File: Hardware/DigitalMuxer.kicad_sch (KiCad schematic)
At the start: 20 parts, among them SW1 Push_Button, SW2 Push_Button, SW3 Push_Button, SW4 Push_Button, SW5 Slide Switch, U2 PCF8574APWR

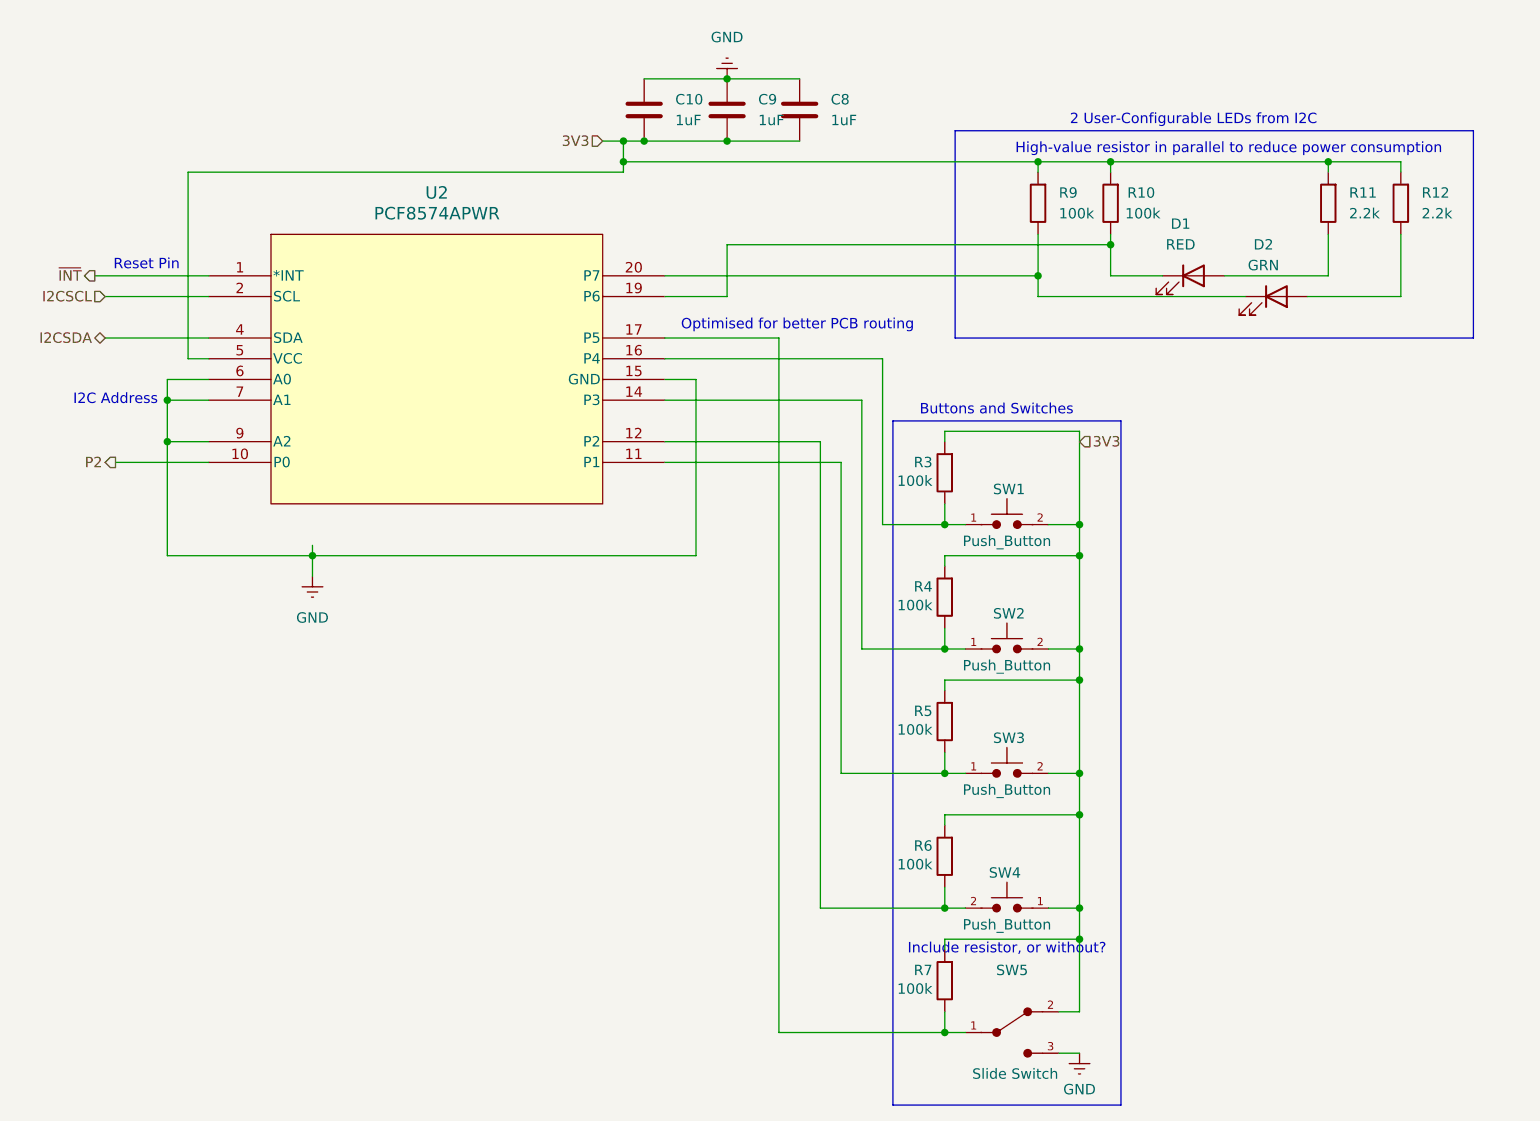
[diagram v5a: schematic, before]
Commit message: Initial OS architecture, and updated PCB work After a joint planning session, designed and architected OS structure: ``` src/ |- os: Audio, Accelerometer, Humidity, etc |- drivers: I2C interfaces, per-chip ```
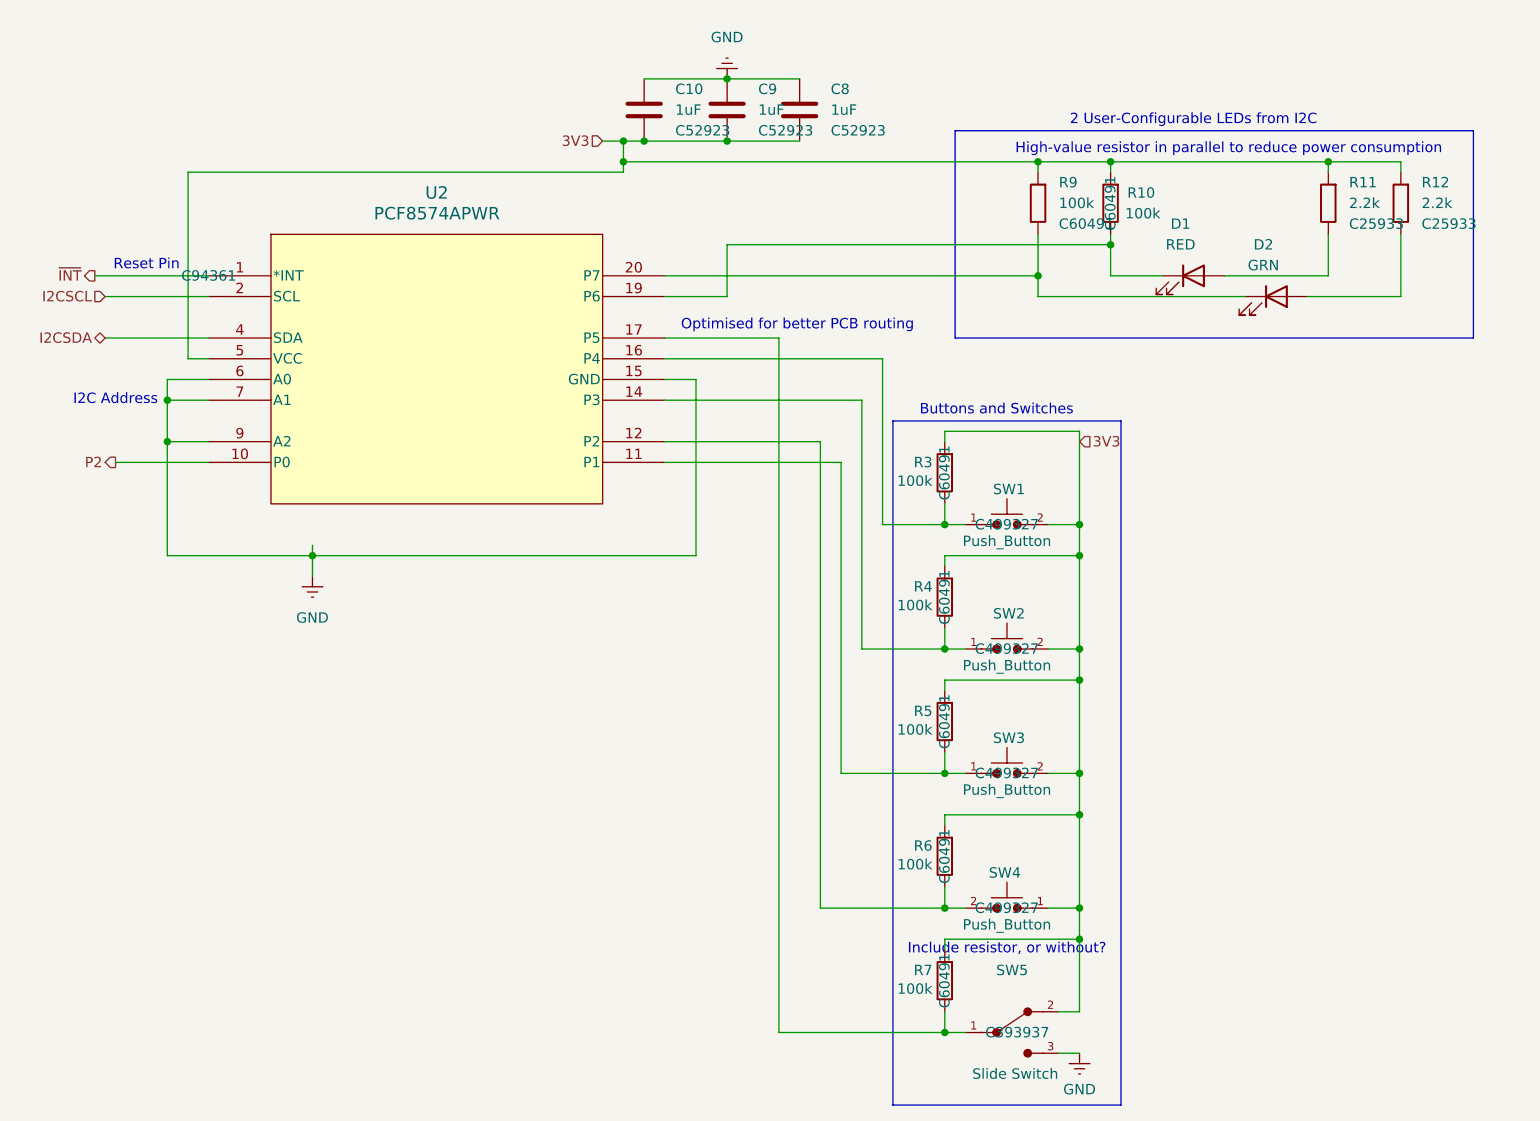
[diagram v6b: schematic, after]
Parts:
- C10, C8, C9: footprint Resistor_SMD:R_01005_0402Metric -> Capacitor_SMD:C_0402_1005Metric; symbol Peanut:C -> Peanut:C 1uF; LCSC (none) -> C52923
- R10, R3, R4, R5, R6, R7, R9: symbol Peanut:R -> Peanut:R 100k; LCSC (none) -> C60491
- R11, R12: symbol Peanut:R -> Peanut:R 2.2k; LCSC (none) -> C25933
- SW1, SW2, SW3, SW4: LCSC (none) -> C499327
- SW5: LCSC (none) -> C393937
- U2: LCSC (none) -> C94361

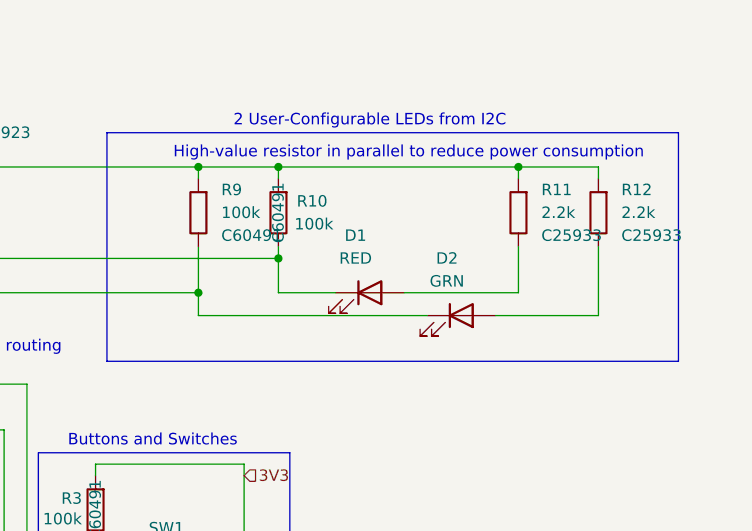
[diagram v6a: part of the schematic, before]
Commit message: Updates to PCB and ADC Schematics
- Swapped audio jack to correct pin (4P-DIP)
- Add LCSC numbers for all components
- Reroute some sensitive signal traces
- Add Board rev and author
- add 4x M2 mounting holes
- fixup some misc silkscreen, footprints, and component 3d models
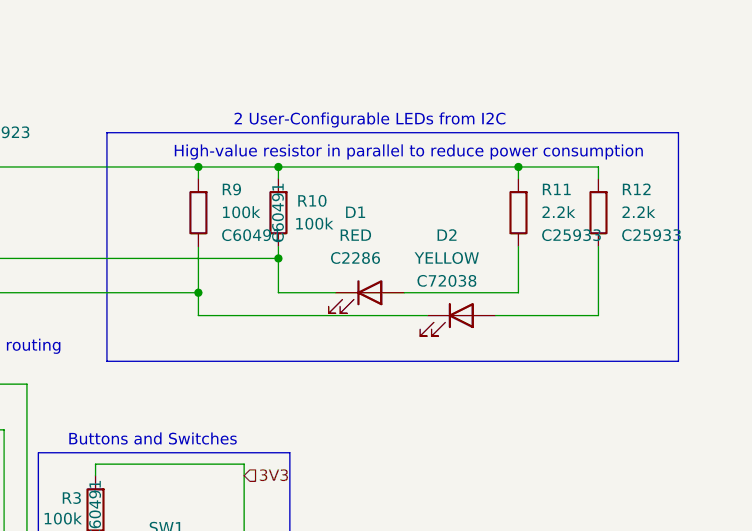
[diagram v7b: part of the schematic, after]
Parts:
- D1: footprint LED_SMD:LED_0201_0603Metric -> LED_SMD:LED_0603_1608Metric; symbol Peanut:LED -> Peanut:LED Red; LCSC (none) -> C2286
- D2: value GRN -> YELLOW; footprint LED_SMD:LED_0201_0603Metric -> LED_SMD:LED_0603_1608Metric; symbol Peanut:LED -> Peanut:LED Yellow; LCSC (none) -> C72038
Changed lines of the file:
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@@
 			)
 		)
-		(property "Description" "Unpolarized capacitor"
+		(property "Description" "Capacitor 1uF"
 			(at 111.76 38.1 0)
 			(effects
@@
 	)
 	(symbol
-		(lib_id "Peanut:LED")
+		(lib_id "Peanut:LED Yellow")
 		(at 179.07 60.96 0)
 		(unit 1)
@@
 		(fields_autoplaced yes)
 		(property "Reference" "D2"
+			(at 177.4825 52.07 0)
+			(effects
+				(font
+					(size 1.27 1.27)
+				)
+			)
+		)
+		(property "Value" "YELLOW"
 			(at 177.4825 54.61 0)
 			(effects
@@
 			)
 		)
-		(property "Value" "GRN"
-			(at 177.4825 57.15 0)
-			(effects
-				(font
-					(size 1.27 1.27)
-				)
-			)
-		)
-		(property "Footprint" "LED_SMD:LED_0201_0603Metric"
+		(property "Footprint" "LED_SMD:LED_0603_1608Metric"
 			(at 179.07 60.96 0)
 			(effects
@@
 			)
 		)
-		(property "Description" "Light emitting diode"
+		(property "Description" "Yellow Light emitting diode"
 			(at 179.07 60.96 0)
 			(effects
@@
 				)
 				(hide yes)
+			)
+		)
+		(property "LCSC" "C72038"
+			(at 177.4825 57.15 0)
+			(effects
+				(font
+					(size 1.27 1.27)
+				)
 			)
 		)
@@
 			)
 		)
-		(property "Description" "Unpolarized capacitor"
+		(property "Description" "Capacitor 1uF"
 			(at 101.6 38.1 0)
 			(effects
@@
 			)
 		)
-		(property "Description" "Unpolarized capacitor"
+		(property "Description" "Capacitor 1uF"
 			(at 120.65 38.1 0)
 			(effects
@@
 	)
 	(symbol
-		(lib_id "Peanut:LED")
+		(lib_id "Peanut:LED Red")
 		(at 168.91 58.42 0)
 		(unit 1)
@@
 		(fields_autoplaced yes)
 		(property "Reference" "D1"
+			(at 167.3225 49.53 0)
+			(effects
+				(font
+					(size 1.27 1.27)
+				)
+			)
+		)
+		(property "Value" "RED"
 			(at 167.3225 52.07 0)
 			(effects
@@
 			)
 		)
-		(property "Value" "RED"
-			(at 167.3225 54.61 0)
-			(effects
-				(font
-					(size 1.27 1.27)
-				)
-			)
-		)
-		(property "Footprint" "LED_SMD:LED_0201_0603Metric"
+		(property "Footprint" "LED_SMD:LED_0603_1608Metric"
 			(at 168.91 58.42 0)
 			(effects
@@
 			)
 		)
-		(property "Description" "Light emitting diode"
+		(property "Description" "Red Light emitting diode"
 			(at 168.91 58.42 0)
 			(effects
@@
 			)
 		)
+		(property "LCSC" "C2286"
+			(at 167.3225 54.61 0)
+			(effects
+				(font
+					(size 1.27 1.27)
+				)
+			)
+		)
